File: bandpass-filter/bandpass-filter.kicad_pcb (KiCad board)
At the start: 2 copper layers, 12 parts

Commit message: Layout done, ready to export to FreeCAD.
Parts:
- moved C5 21.1 mm to (95.9, 57.0), turned to -90 degrees
- moved L5 20.6 mm to (97.5, 57.0), turned to 90 degrees
- moved TP1 20.3 mm to (81.5, 56.3)
- moved C4 18.0 mm to (92.8, 57.0), turned to -90 degrees
- moved L4 17.9 mm to (94.4, 57.0), turned to -90 degrees
- moved L3 15.8 mm to (91.3, 57.0), turned to 90 degrees
- moved C3 15.5 mm to (89.7, 57.0), turned to -90 degrees
- moved L2 14.5 mm to (88.2, 57.0), turned to -90 degrees
- moved TP2 14.5 mm to (99.5, 56.3)
- moved L1 14.2 mm to (85.0, 57.0), turned to 90 degrees
- moved C2 13.6 mm to (86.6, 57.0), turned to -90 degrees
- moved C1 12.7 mm to (83.5, 57.0), turned to -90 degrees
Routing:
- net Net-(C2-Pad1): track 0.00 -> 4.69 mm
- net Net-(C4-Pad1): track 0.00 -> 4.69 mm
- net /out: track 0.00 -> 2.03 mm
- net /in: track 0.00 -> 2.02 mm
- net Net-(C5-Pad2): track 0.00 -> 1.56 mm
- net Net-(C1-Pad2): track 0.00 -> 1.56 mm
- net Net-(C3-Pad2): track 0.00 -> 1.56 mm
- net 0: vias 0 -> 4
- added copper zone on B.Cu, net 0
- added copper zone on F.Cu, net 0
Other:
- board outline added: 21 x 7 mm

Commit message: Changing PCB layout.
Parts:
- C1, C5: value 5.6pF -> 5.6p
- C2, C4: value 220pF -> 220p
- C3: value 3.3pF -> 3.3p
- L1, L5: value 470nH -> 470n
- L2, L4: value 12nH -> 12n
- L3: value 820nF -> 820n
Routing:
- net 0: vias 4 -> 17
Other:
- board text added: "0"
- board text added: "0 mm"
- board text added: "0.01 mm"
- board text added: "0.02"
- board text added: "0.035 mm"
- board text added: "0.1000 mm / 0.1000 mm"
- board text added: "0.3000 mm"
- board text added: "0.93 mm"
- board text added: "1"
- board text added: "1.0200 mm"
- board text added: "2"
- board text added: "21.0000 mm x 7.0000 mm"
- board text added: "3.3"
- board text added: "4.5"
- board text added: "B.Cu"
- board text added: "B.Mask"
- board text added: "B.Paste"
- board text added: "B.Silkscreen"
- board text added: "BOARD CHARACTERISTICS"
- board text added: "Board Thickness:"
- board text added: "Board overall dimensions:"
- board text added: "Bottom Silk Screen"
- board text added: "Bottom Solder Mask"
- board text added: "Bottom Solder Paste"
- board text added: "Castellated pads:"
- board text added: "Color"
- board text added: "Copper Finish:"
- board text added: "Copper Layer Count:"
- board text added: "Dielectric"
- board text added: "Edge card connectors:"
- board text added: "Epsilon R"
- board text added: "F.Cu"
- board text added: "F.Mask"
- board text added: "F.Paste"
- board text added: "F.Silkscreen"
- board text added: "FR4"
- board text added: "FR4 natural"
- board text added: "Green"
- board text added: "Impedance Control:"
- board text added: "Layer Name"
- board text added: "Liquid Ink"
- board text added: "Liquid Photo"
- board text added: "Loss Tangent"
- board text added: "Material"
- board text added: "Min hole diameter:"
- board text added: "Min track/spacing:"
- board text added: "No"
- board text added: "None"
- board text added: "Plated Board Edge:"
- board text added: "Thickness (mm)"
- board text added: "Top Silk Screen"
- board text added: "Top Solder Mask"
- board text added: "Top Solder Paste"
- board text added: "Type"
- board text added: "White"
- board text added: "Yellow"
- board text added: "copper"
- board text added: "core"

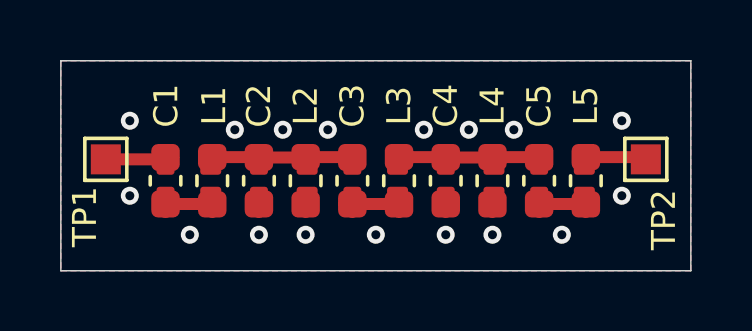
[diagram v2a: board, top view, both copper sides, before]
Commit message: CHanging top layer model for compacting mesh.
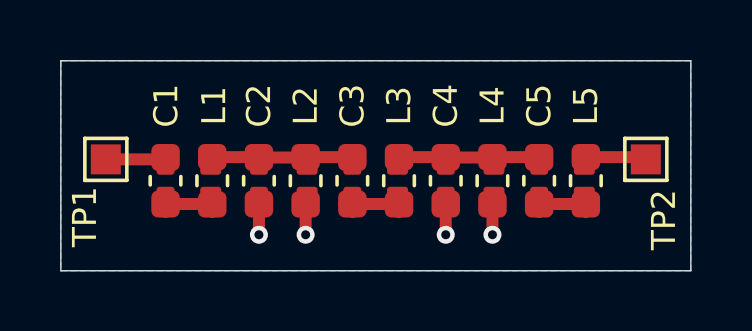
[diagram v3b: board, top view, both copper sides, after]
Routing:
- net 0: track 0.00 -> 4.07 mm, vias 17 -> 4
- removed copper zone on F.Cu, net 0
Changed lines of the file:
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@@
 		(net 2)
+	)
+	(segment
+		(start 94.386667 57.787501)
+		(end 94.386667 58.8)
+		(width 0.4)
+		(layer "F.Cu")
+		(net 3)
+	)
+	(segment
+		(start 86.603333 57.775)
+		(end 86.603333 58.8)
+		(width 0.4)
+		(layer "F.Cu")
+		(net 3)
+	)
+	(segment
+		(start 88.16 57.787501)
+		(end 88.16 58.8)
+		(width 0.4)
+		(layer "F.Cu")
+		(net 3)
+	)
+	(segment
+		(start 92.83 57.775)
+		(end 92.83 58.8)
+		(width 0.4)
+		(layer "F.Cu")
+		(net 3)
 	)
 	(via
 		(at 94.386667 58.8)
-		(size 0.6)
-		(drill 0.3)
-		(layers "F.Cu" "B.Cu")
-		(free yes)
-		(net 3)
-	)
-	(via
-		(at 92.1 55.3)
-		(size 0.6)
-		(drill 0.3)
-		(layers "F.Cu" "B.Cu")
-		(free yes)
-		(net 3)
-	)
-	(via
-		(at 85.8 55.3)
-		(size 0.6)
-		(drill 0.3)
-		(layers "F.Cu" "B.Cu")
-		(free yes)
-		(net 3)
-	)
-	(via
-		(at 88.9 55.3)
-		(size 0.6)
-		(drill 0.3)
-		(layers "F.Cu" "B.Cu")
-		(free yes)
-		(net 3)
-	)
-	(via
-		(at 95.1 55.3)
 		(size 0.6)
 		(drill 0.3)
@@
 	)
 	(via
-		(at 96.7 58.8)
-		(size 0.6)
-		(drill 0.3)
-		(layers "F.Cu" "B.Cu")
-		(free yes)
-		(net 3)
-	)
-	(via
-		(at 84.3 58.8)
-		(size 0.6)
-		(drill 0.3)
-		(layers "F.Cu" "B.Cu")
-		(free yes)
-		(net 3)
-	)
-	(via
 		(at 92.83 58.8)
-		(size 0.6)
-		(drill 0.3)
-		(layers "F.Cu" "B.Cu")
-		(free yes)
-		(net 3)
-	)
-	(via
-		(at 98.7 57.5)
-		(size 0.6)
-		(drill 0.3)
-		(layers "F.Cu" "B.Cu")
-		(free yes)
-		(net 3)
-	)
-	(via
-		(at 82.3 57.5)
-		(size 0.6)
-		(drill 0.3)
-		(layers "F.Cu" "B.Cu")
-		(free yes)
-		(net 3)
-	)
-	(via
-		(at 90.5 58.8)
-		(size 0.6)
-		(drill 0.3)
-		(layers "F.Cu" "B.Cu")
-		(free yes)
-		(net 3)
-	)
-	(via
-		(at 98.7 55)
-		(size 0.6)
-		(drill 0.3)
-		(layers "F.Cu" "B.Cu")
-		(free yes)
-		(net 3)
-	)
-	(via
-		(at 87.4 55.3)
-		(size 0.6)
-		(drill 0.3)
-		(layers "F.Cu" "B.Cu")
-		(free yes)
-		(net 3)
-	)
-	(via
-		(at 82.3 55)
-		(size 0.6)
-		(drill 0.3)
-		(layers "F.Cu" "B.Cu")
-		(free yes)
-		(net 3)
-	)
-	(via
-		(at 93.6 55.3)
 		(size 0.6)
 		(drill 0.3)
@@
 		(net 3)
 		(net_name "0")
-		(layers "F.Cu" "B.Cu")
+		(layer "B.Cu")
 		(hatch edge 0.1)
 		(connect_pads
